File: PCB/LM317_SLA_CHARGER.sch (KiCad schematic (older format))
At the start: 6 parts, among them U4 LM317DCYR

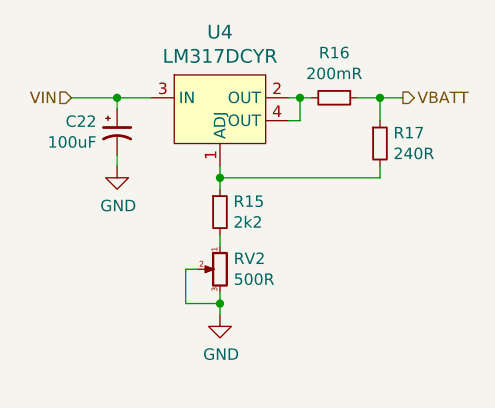
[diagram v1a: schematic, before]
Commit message: Added Humidity and temperature sensors
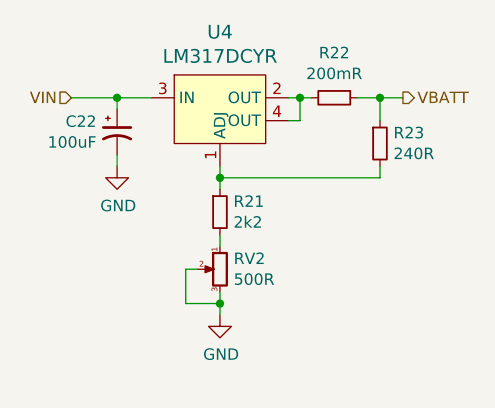
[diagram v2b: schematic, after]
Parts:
- renumbered R15 to R21, R16 to R22, R17 to R23
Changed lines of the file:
@@
 	5250 3600 5400 3600
 $Comp
-L power:GND #PWR070
+L power:GND #PWR073
 U 1 1 5E995485
 P 5250 3900
-F 0 "#PWR070" H 5250 3650 50  0001 C CNN
+F 0 "#PWR073" H 5250 3650 50  0001 C CNN
 F 1 "GND" H 5255 3727 50  0000 C CNN
 F 2 "" H 5250 3900 50  0001 C CNN
@@
 	5250 3900 5250 3850
 $Comp
-L Device:R_Small R16
+L Device:R_Small R22
 U 1 1 5E995CBE
 P 6200 3600
-F 0 "R16" V 6004 3600 50  0000 C CNN
+F 0 "R22" V 6004 3600 50  0000 C CNN
 F 1 "200mR" V 6095 3600 50  0000 C CNN
 F 2 "" H 6200 3600 50  0001 C CNN
@@
 	6050 3600 6100 3600
 $Comp
-L Device:R_Small R17
+L Device:R_Small R23
 U 1 1 5E9965CD
 P 6400 3800
-F 0 "R17" H 6459 3846 50  0000 L CNN
+F 0 "R23" H 6459 3846 50  0000 L CNN
 F 1 "240R" H 6459 3755 50  0000 L CNN
 F 2 "" H 6400 3800 50  0001 C CNN
@@
 $EndComp
 $Comp
-L Device:R_Small R15
+L Device:R_Small R21
 U 1 1 5E9966F3
 P 5700 4100
-F 0 "R15" H 5759 4146 50  0000 L CNN
+F 0 "R21" H 5759 4146 50  0000 L CNN
 F 1 "2k2" H 5759 4055 50  0000 L CNN
 F 2 "" H 5700 4100 50  0001 C CNN
@@
 $EndComp
 $Comp
-L power:GND #PWR071
+L power:GND #PWR074
 U 1 1 5E996838
 P 5700 4550
-F 0 "#PWR071" H 5700 4300 50  0001 C CNN
+F 0 "#PWR074" H 5700 4300 50  0001 C CNN
 F 1 "GND" H 5705 4377 50  0000 C CNN
 F 2 "" H 5700 4550 50  0001 C CNN

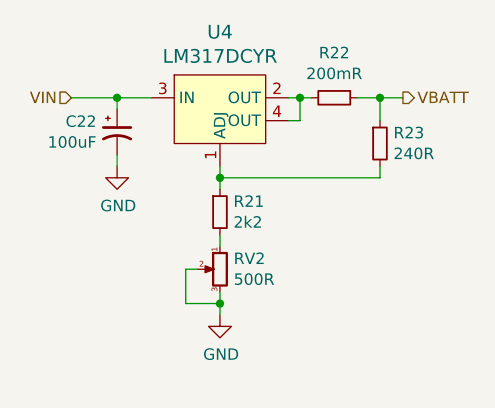
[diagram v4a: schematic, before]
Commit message: Added remaining test points
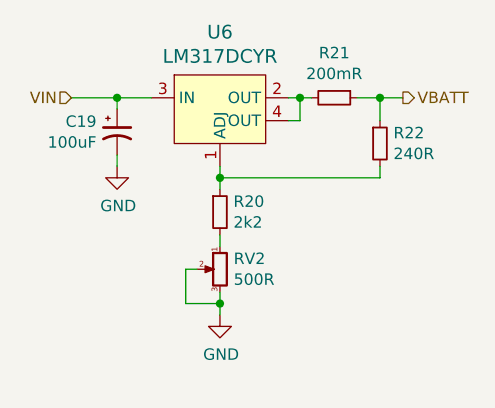
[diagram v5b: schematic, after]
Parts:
- renumbered C22 to C19, R21 to R20, R22 to R21, R23 to R22, U4 to U6
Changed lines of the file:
@@
 VBATT
 $Comp
-L dk_PMIC-Voltage-Regulators-Linear:LM317DCYR U4
+L dk_PMIC-Voltage-Regulators-Linear:LM317DCYR U6
 U 1 1 5E993DB7
 P 5700 3600
-F 0 "U4" H 5700 3887 60  0000 C CNN
+F 0 "U6" H 5700 3887 60  0000 C CNN
 F 1 "LM317DCYR" H 5700 3781 60  0000 C CNN
 F 2 "digikey-footprints:SOT-223-4" H 5900 3800 60  0001 L CNN
@@
 $EndComp
 $Comp
-L Device:CP1_Small C22
+L Device:CP1_Small C19
 U 1 1 5E9947F2
 P 5250 3750
-F 0 "C22" H 5160 3796 50  0000 R CNN
+F 0 "C19" H 5160 3796 50  0000 R CNN
 F 1 "100uF" H 5160 3705 50  0000 R CNN
 F 2 "" H 5250 3750 50  0001 C CNN
@@
 	5250 3600 5400 3600
 $Comp
-L power:GND #PWR073
+L power:GND #PWR069
 U 1 1 5E995485
 P 5250 3900
-F 0 "#PWR073" H 5250 3650 50  0001 C CNN
+F 0 "#PWR069" H 5250 3650 50  0001 C CNN
 F 1 "GND" H 5255 3727 50  0000 C CNN
 F 2 "" H 5250 3900 50  0001 C CNN
@@
 	5250 3900 5250 3850
 $Comp
-L Device:R_Small R22
+L Device:R_Small R21
 U 1 1 5E995CBE
 P 6200 3600
-F 0 "R22" V 6004 3600 50  0000 C CNN
+F 0 "R21" V 6004 3600 50  0000 C CNN
 F 1 "200mR" V 6095 3600 50  0000 C CNN
 F 2 "" H 6200 3600 50  0001 C CNN
@@
 	6050 3600 6100 3600
 $Comp
-L Device:R_Small R23
+L Device:R_Small R22
 U 1 1 5E9965CD
 P 6400 3800
-F 0 "R23" H 6459 3846 50  0000 L CNN
+F 0 "R22" H 6459 3846 50  0000 L CNN
 F 1 "240R" H 6459 3755 50  0000 L CNN
 F 2 "" H 6400 3800 50  0001 C CNN
@@
 $EndComp
 $Comp
-L Device:R_Small R21
+L Device:R_Small R20
 U 1 1 5E9966F3
 P 5700 4100
-F 0 "R21" H 5759 4146 50  0000 L CNN
+F 0 "R20" H 5759 4146 50  0000 L CNN
 F 1 "2k2" H 5759 4055 50  0000 L CNN
 F 2 "" H 5700 4100 50  0001 C CNN
@@
 $EndComp
 $Comp
-L power:GND #PWR074
+L power:GND #PWR070
 U 1 1 5E996838
 P 5700 4550
-F 0 "#PWR074" H 5700 4300 50  0001 C CNN
+F 0 "#PWR070" H 5700 4300 50  0001 C CNN
 F 1 "GND" H 5705 4377 50  0000 C CNN
 F 2 "" H 5700 4550 50  0001 C CNN

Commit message: Added RV bypass jumper to SLA charger
In production this can be jumped and the current set resistor pair adjusted in order to remove the need for the pot
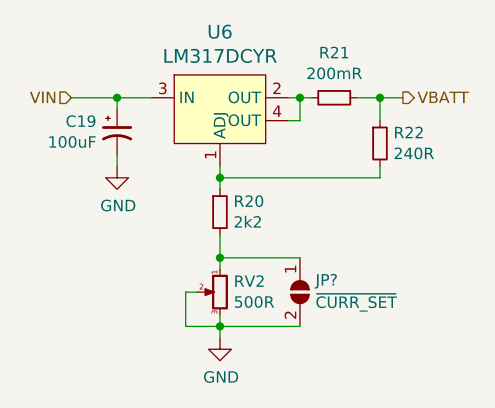
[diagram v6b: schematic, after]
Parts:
- added JP?: ~CURR_SET, symbol Jumper:SolderJumper_2_Open
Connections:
- net GND: now also JP?.2 (B)
- net at R20.2, RV2.1: now also JP?.1 (A)
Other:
- moved on the sheet: RV2
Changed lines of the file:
@@
 L power:GND #PWR070
 U 1 1 5E996838
-P 5700 4550
-F 0 "#PWR070" H 5700 4300 50  0001 C CNN
-F 1 "GND" H 5705 4377 50  0000 C CNN
-F 2 "" H 5700 4550 50  0001 C CNN
-F 3 "" H 5700 4550 50  0001 C CNN
-	1    5700 4550
+P 5700 4650
+F 0 "#PWR070" H 5700 4400 50  0001 C CNN
+F 1 "GND" H 5705 4477 50  0000 C CNN
+F 2 "" H 5700 4650 50  0001 C CNN
+F 3 "" H 5700 4650 50  0001 C CNN
+	1    5700 4650
 	1    0    0    -1
 $EndComp
 Wire Wire Line
-	5700 4200 5700 4250
+	5700 4200 5700 4300
 Wire Wire Line
 	5700 3900 5700 3950
@@
 L Device:R_POT_Small RV2
 U 1 1 5E9991C6
-P 5700 4350
-F 0 "RV2" H 5640 4396 50  0000 R CNN
-F 1 "500R" H 5640 4305 50  0000 R CNN
-F 2 "" H 5700 4350 50  0001 C CNN
-F 3 "" H 5700 4350 50  0001 C CNN
-	1    5700 4350
+P 5700 4450
+F 0 "RV2" H 5640 4496 50  0000 R CNN
+F 1 "500R" H 5640 4405 50  0000 R CNN
+F 2 "" H 5700 4450 50  0001 C CNN
+F 3 "" H 5700 4450 50  0001 C CNN
+	1    5700 4450
 	-1   0    0    -1
 $EndComp
 Wire Wire Line
-	5700 4450 5700 4500
+	5700 4550 5700 4600
 Wire Wire Line
-	5600 4350 5550 4350
+	5600 4450 5550 4450
 Wire Wire Line
-	5550 4350 5550 4500
+	5550 4450 5550 4600
 Wire Wire Line
-	5550 4500 5700 4500
-Connection ~ 5700 4500
+	5550 4600 5700 4600
+Connection ~ 5700 4600
 Wire Wire Line
-	5700 4500 5700 4550
+	5700 4600 5700 4650
+$Comp
+L Jumper:SolderJumper_2_Open JP?
+U 1 1 5E9F21F4
+P 6050 4450
+F 0 "JP?" V 5998 4518 50  0000 L CNN
+F 1 "~CURR_SET" V 6096 4518 50  0000 L CNN
+F 2 "" H 6050 4450 50  0001 C CNN
+F 3 "~" H 6050 4450 50  0001 C CNN
+	1    6050 4450
+	0    1    1    0
+$EndComp
+Wire Wire Line
+	6050 4600 5700 4600
+Wire Wire Line
+	6050 4300 5700 4300
+Connection ~ 5700 4300
+Wire Wire Line
+	5700 4300 5700 4350
 $EndSCHEMATC

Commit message: Added PDF schematic
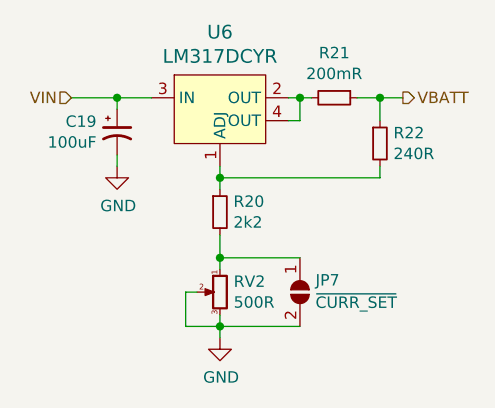
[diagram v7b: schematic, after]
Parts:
- gave numbers to parts that had none: 1
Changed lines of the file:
@@
 	5700 4600 5700 4650
 $Comp
-L Jumper:SolderJumper_2_Open JP?
+L Jumper:SolderJumper_2_Open JP7
 U 1 1 5E9F21F4
 P 6050 4450
-F 0 "JP?" V 5998 4518 50  0000 L CNN
+F 0 "JP7" V 5998 4518 50  0000 L CNN
 F 1 "~CURR_SET" V 6096 4518 50  0000 L CNN
 F 2 "" H 6050 4450 50  0001 C CNN

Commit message: Added majority footprints
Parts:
- C19: footprint (none) -> Capacitor_SMD:CP_Elec_5x5.4
- JP7: footprint (none) -> Jumpers:SMT-JUMPER_2_NO_SILK
- R20, R22: footprint (none) -> Resistor_SMD:R_0603_1608Metric
- R21: footprint (none) -> Resistor_SMD:R_0805_2012Metric; Power Rating (none) -> 1/4W
- U6: footprint digikey-footprints:SOT-223-4 -> Package_TO_SOT_SMD:SOT-223
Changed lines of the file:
@@
 F 0 "U6" H 5700 3887 60  0000 C CNN
 F 1 "LM317DCYR" H 5700 3781 60  0000 C CNN
-F 2 "digikey-footprints:SOT-223-4" H 5900 3800 60  0001 L CNN
+F 2 "Package_TO_SOT_SMD:SOT-223" H 5900 3800 60  0001 L CNN
 F 3 "http://www.ti.com/general/docs/suppproductinfo.tsp?distId=10&gotoUrl=http%3A%2F%2Fwww.ti.com%2Flit%2Fgpn%2Flm317" H 5900 3900 60  0001 L CNN
 F 4 "LM317DCYR" H 5900 4100 60  0001 L CNN "MPN"
@@
 F 0 "C19" H 5160 3796 50  0000 R CNN
 F 1 "100uF" H 5160 3705 50  0000 R CNN
-F 2 "" H 5250 3750 50  0001 C CNN
+F 2 "Capacitor_SMD:CP_Elec_5x5.4" H 5250 3750 50  0001 C CNN
 F 3 "" H 5250 3750 50  0001 C CNN
 F 4 "Aluminium Film" H 5250 3750 50  0001 C CNN "Dielectric"
@@
 F 0 "R21" V 6004 3600 50  0000 C CNN
 F 1 "200mR" V 6095 3600 50  0000 C CNN
-F 2 "" H 6200 3600 50  0001 C CNN
+F 2 "Resistor_SMD:R_0805_2012Metric" H 6200 3600 50  0001 C CNN
 F 3 "" H 6200 3600 50  0001 C CNN
+F 4 "1/4W" V 6200 3600 50  0001 C CNN "Power Rating"
 	1    6200 3600
 	0    1    1    0
@@
 F 0 "R22" H 6459 3846 50  0000 L CNN
 F 1 "240R" H 6459 3755 50  0000 L CNN
-F 2 "" H 6400 3800 50  0001 C CNN
+F 2 "Resistor_SMD:R_0603_1608Metric" H 6400 3800 50  0001 C CNN
 F 3 "" H 6400 3800 50  0001 C CNN
 	1    6400 3800
@@
 F 0 "R20" H 5759 4146 50  0000 L CNN
 F 1 "2k2" H 5759 4055 50  0000 L CNN
-F 2 "" H 5700 4100 50  0001 C CNN
+F 2 "Resistor_SMD:R_0603_1608Metric" H 5700 4100 50  0001 C CNN
 F 3 "" H 5700 4100 50  0001 C CNN
 	1    5700 4100
@@
 F 0 "JP7" V 5998 4518 50  0000 L CNN
 F 1 "~CURR_SET" V 6096 4518 50  0000 L CNN
-F 2 "" H 6050 4450 50  0001 C CNN
+F 2 "Jumpers:SMT-JUMPER_2_NO_SILK" H 6050 4450 50  0001 C CNN
 F 3 "~" H 6050 4450 50  0001 C CNN
 	1    6050 4450
